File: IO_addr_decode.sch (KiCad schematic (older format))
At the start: 5 parts

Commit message: Fix wiring in root sheet
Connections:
- net ~CS_SSD1 renamed ~CS_7_SEG_0
- net ~CS_SSD2 renamed ~CS_7_SEG_1
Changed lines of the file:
@@
 $Descr A4 11693 8268
 encoding utf-8
-Sheet 14 14
+Sheet 14 15
 Title "IO Address Decode"
 Date ""
@@
 AR Path="/61AA766E/61AA7D4D" Ref="U?"  Part="1"
 AR Path="/61B01AF5/61AA7D4D" Ref="U?"  Part="1"
+AR Path="/61ABA723/61AA7D4D" Ref="U?"  Part="1"
 F 0 "U?" H 3825 3525 50  0000 C CNN
 F 1 "74LS30" H 3825 3434 50  0000 C CNN
@@
 AR Path="/61AA766E/61ABC77F" Ref="#PWR?"  Part="1"
 AR Path="/61B01AF5/61ABC77F" Ref="#PWR?"  Part="1"
+AR Path="/61ABA723/61ABC77F" Ref="#PWR?"  Part="1"
 F 0 "#PWR?" H 7500 3375 50  0001 C CNN
 F 1 "GND" H 7505 3452 50  0000 C CNN
@@
 AR Path="/61AA766E/61ABC361" Ref="#PWR?"  Part="1"
 AR Path="/61B01AF5/61ABC361" Ref="#PWR?"  Part="1"
+AR Path="/61ABA723/61ABC361" Ref="#PWR?"  Part="1"
 F 0 "#PWR?" H 7500 2175 50  0001 C CNN
 F 1 "VCC" H 7515 2498 50  0000 C CNN
@@
 AR Path="/61AA766E/61AC4663" Ref="#PWR?"  Part="1"
 AR Path="/61B01AF5/61AC4663" Ref="#PWR?"  Part="1"
+AR Path="/61ABA723/61AC4663" Ref="#PWR?"  Part="1"
 F 0 "#PWR?" H 7500 5225 50  0001 C CNN
 F 1 "GND" H 7505 5302 50  0000 C CNN
@@
 AR Path="/61AA766E/61AC466D" Ref="#PWR?"  Part="1"
 AR Path="/61B01AF5/61AC466D" Ref="#PWR?"  Part="1"
+AR Path="/61ABA723/61AC466D" Ref="#PWR?"  Part="1"
 F 0 "#PWR?" H 7500 4025 50  0001 C CNN
 F 1 "VCC" H 7515 4348 50  0000 C CNN
@@
 AR Path="/61AA766E/61AC4691" Ref="U?"  Part="1"
 AR Path="/61B01AF5/61AC4691" Ref="U?"  Part="1"
+AR Path="/61ABA723/61AC4691" Ref="U?"  Part="1"
 F 0 "U?" H 7250 5625 50  0000 C CNN
 F 1 "PAL16L8" H 7250 5525 50  0000 C CNN
@@
 AR Path="/61AA766E/61AAD950" Ref="U?"  Part="1"
 AR Path="/61B01AF5/61AAD950" Ref="U?"  Part="1"
+AR Path="/61ABA723/61AAD950" Ref="U?"  Part="1"
 F 0 "U?" H 7250 3775 50  0000 C CNN
 F 1 "PAL16L8" H 7250 3675 50  0000 C CNN
@@
 ~CS_LCD
 Text HLabel 8000 4375 2    50   Output ~ 0
-~CS_SSD1
+~CS_7_SEG_0
 Text HLabel 8000 4475 2    50   Output ~ 0
-~CS_SSD2
+~CS_7_SEG_1
 Text HLabel 8000 4575 2    50   Output ~ 0
 ~CS_LED
@@
 AR Path="/61AA766E/61AEBFAB" Ref="C?"  Part="1"
 AR Path="/61B01AF5/61AEBFAB" Ref="C?"  Part="1"
+AR Path="/61ABA723/61AEBFAB" Ref="C?"  Part="1"
 F 0 "C?" H 3365 5046 50  0000 L CNN
 F 1 "100nF" H 3365 4955 50  0000 L CNN
@@
 AR Path="/61AA766E/61AEC48E" Ref="C?"  Part="1"
 AR Path="/61B01AF5/61AEC48E" Ref="C?"  Part="1"
+AR Path="/61ABA723/61AEC48E" Ref="C?"  Part="1"
 F 0 "C?" H 3865 5046 50  0000 L CNN
 F 1 "100nF" H 3865 4955 50  0000 L CNN
@@
 AR Path="/61AA766E/61AF08F7" Ref="#PWR?"  Part="1"
 AR Path="/61B01AF5/61AF08F7" Ref="#PWR?"  Part="1"
+AR Path="/61ABA723/61AF08F7" Ref="#PWR?"  Part="1"
 F 0 "#PWR?" H 3500 4900 50  0001 C CNN
 F 1 "GND" H 3505 4977 50  0000 C CNN
@@
 AR Path="/61AA766E/61AF0CA8" Ref="#PWR?"  Part="1"
 AR Path="/61B01AF5/61AF0CA8" Ref="#PWR?"  Part="1"
+AR Path="/61ABA723/61AF0CA8" Ref="#PWR?"  Part="1"
 F 0 "#PWR?" H 3500 4700 50  0001 C CNN
 F 1 "VCC" H 3515 5023 50  0000 C CNN

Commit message: Decode BHE for IO addresses
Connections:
- net ~CS_LCD: now also U?.15 (IO5); no longer U?.12 (IO8)
- net ~CS_UART: now also U?.14 (IO6); no longer U?.13 (IO7)
- net ~BHE: now reaches U?.12 (IO8)
- net ~BHE: now also U?.12 (IO8)
- no-connect marks 4 -> 2
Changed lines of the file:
@@
 	1    0    0    -1
 $EndComp
-NoConn ~ 8000 5075
 Text HLabel 8000 2525 2    50   Output ~ 0
 ~CS_PPI1
@@
 Text HLabel 8000 3025 2    50   Output ~ 0
 ~CS_KBRD
-Text HLabel 8000 3125 2    50   Output ~ 0
+Text HLabel 8000 4875 2    50   Output ~ 0
 ~CS_UART
-Text HLabel 8000 3225 2    50   Output ~ 0
+Text HLabel 8000 4775 2    50   Output ~ 0
 ~CS_LCD
 Text HLabel 8000 4375 2    50   Output ~ 0
@@
 Text HLabel 8000 4675 2    50   Output ~ 0
 ~CS_SW
-NoConn ~ 8000 4775
-NoConn ~ 8000 4875
 NoConn ~ 8000 4975
 $Comp
@@
 Text Notes 6875 1950 0    50   ~ 0
 16L8 PAL: decode low byte
+NoConn ~ 8000 3125
 Wire Bus Line
 	6675 4150 6675 4975
@@
 Wire Bus Line
 	3200 2475 3200 3300
+Text HLabel 8000 3225 2    50   Input ~ 0
+~BHE
+Text HLabel 8000 5075 2    50   Input ~ 0
+~BHE
 $EndSCHEMATC

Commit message: General edits; removed floating inputs
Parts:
- added U?: 74LS30, symbol 74xx:74LS30
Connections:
- net HI_BYTE_FF is gone; now on net ~HI_BYTE_FF: U?.9 (I9)
- net GND: now also U?.7 (GND)
- net VCC: now also U?.14 (VCC)
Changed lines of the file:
@@
 ~HI_BYTE_FF
 Text Label 7000 5175 2    50   ~ 0
-HI_BYTE_FF
+~HI_BYTE_FF
 $Comp
 L Logic_Programmable:PAL16L8 U?
@@
 16L8 PAL: decode low byte
 NoConn ~ 8000 3125
+Text HLabel 8000 3225 2    50   Input ~ 0
+~BHE
+Text HLabel 8000 5075 2    50   Input ~ 0
+~BHE
+$Comp
+L 74xx:74LS30 U?
+U 2 1 61F51AA5
+P 4550 5050
+F 0 "U?" H 4780 5096 50  0000 L CNN
+F 1 "74LS30" H 4780 5005 50  0000 L CNN
+F 2 "" H 4550 5050 50  0001 C CNN
+F 3 "http://www.ti.com/lit/gpn/sn74LS30" H 4550 5050 50  0001 C CNN
+	2    4550 5050
+	1    0    0    -1
+$EndComp
+Wire Wire Line
+	4550 4550 3750 4550
+Wire Wire Line
+	3750 4550 3750 4850
+Connection ~ 3750 4850
+Wire Wire Line
+	4550 5550 3750 5550
+Wire Wire Line
+	3750 5550 3750 5150
 Wire Bus Line
 	6675 4150 6675 4975
@@
 Wire Bus Line
 	3200 2475 3200 3300
-Text HLabel 8000 3225 2    50   Input ~ 0
-~BHE
-Text HLabel 8000 5075 2    50   Input ~ 0
-~BHE
+Connection ~ 3750 5150
 $EndSCHEMATC

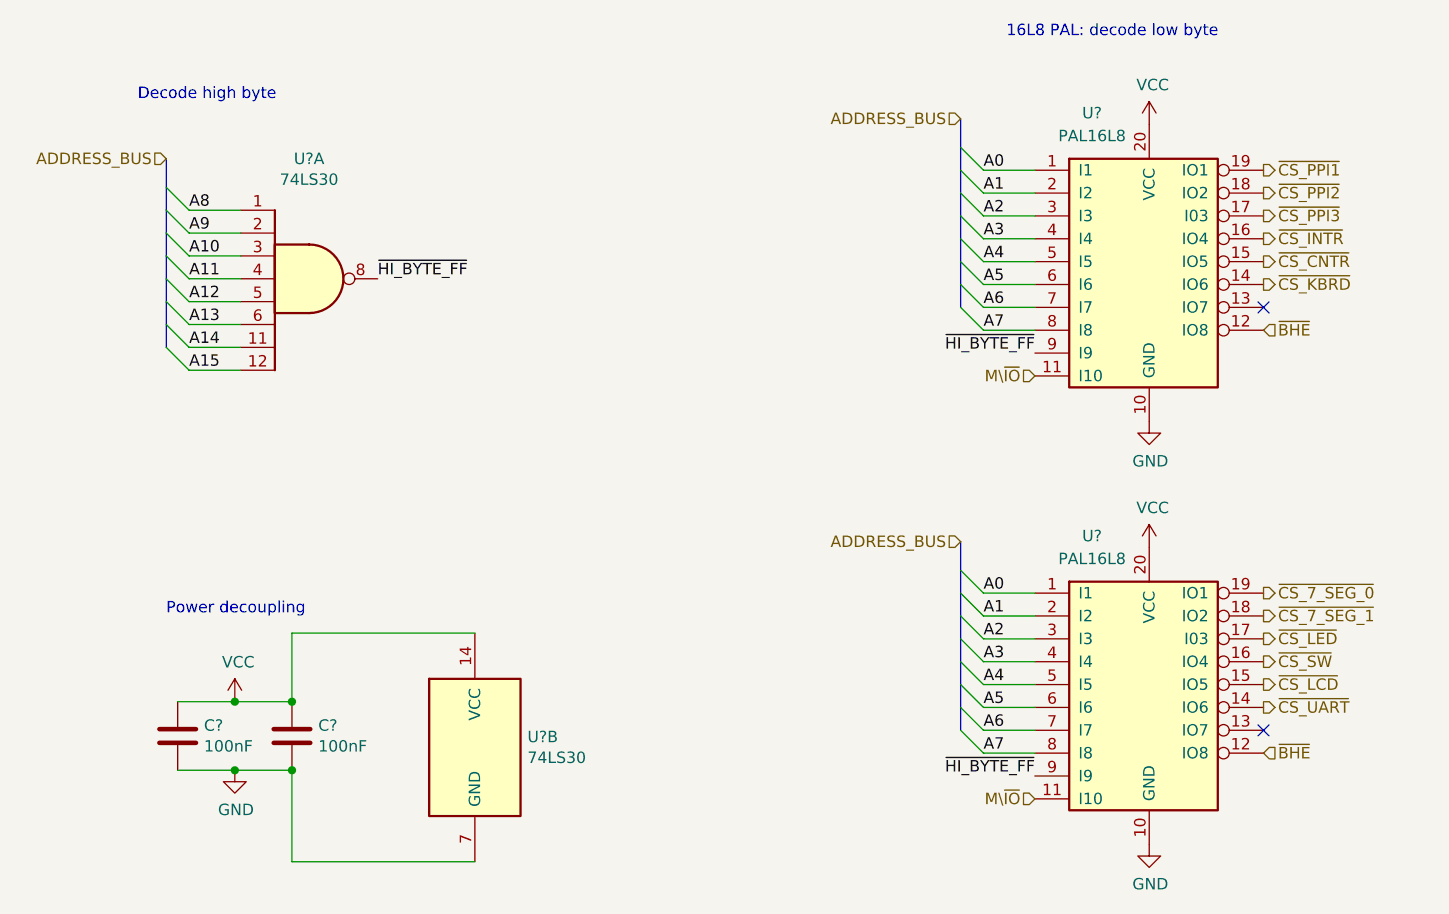
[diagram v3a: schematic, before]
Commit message: Updates to pass ERC
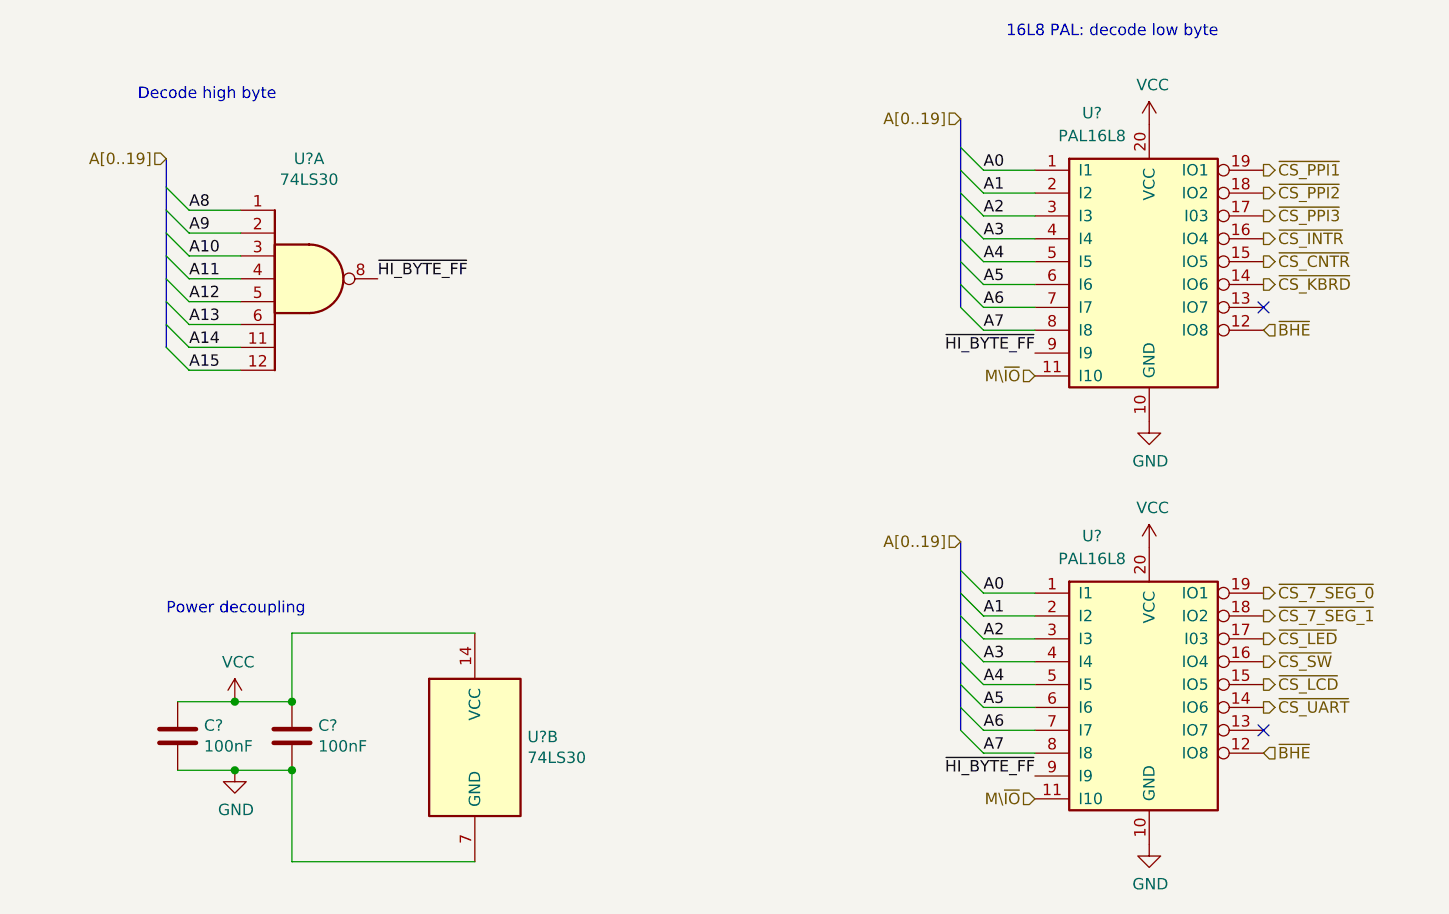
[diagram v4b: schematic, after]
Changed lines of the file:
@@
 $EndComp
 Text HLabel 3200 2475 0    50   Input ~ 0
-ADDRESS_BUS
+A[0..19]
 Text Label 4125 3000 0    50   ~ 0
 ~HI_BYTE_FF
@@
 M\~IO
 Text HLabel 6675 2300 0    50   Input ~ 0
-ADDRESS_BUS
+A[0..19]
 Entry Wire Line
 	6675 3125 6775 3225
@@
 M\~IO
 Text HLabel 6675 4150 0    50   Input ~ 0
-ADDRESS_BUS
+A[0..19]
 Entry Wire Line
 	6675 4975 6775 5075

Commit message: Assign footprints for most symbols
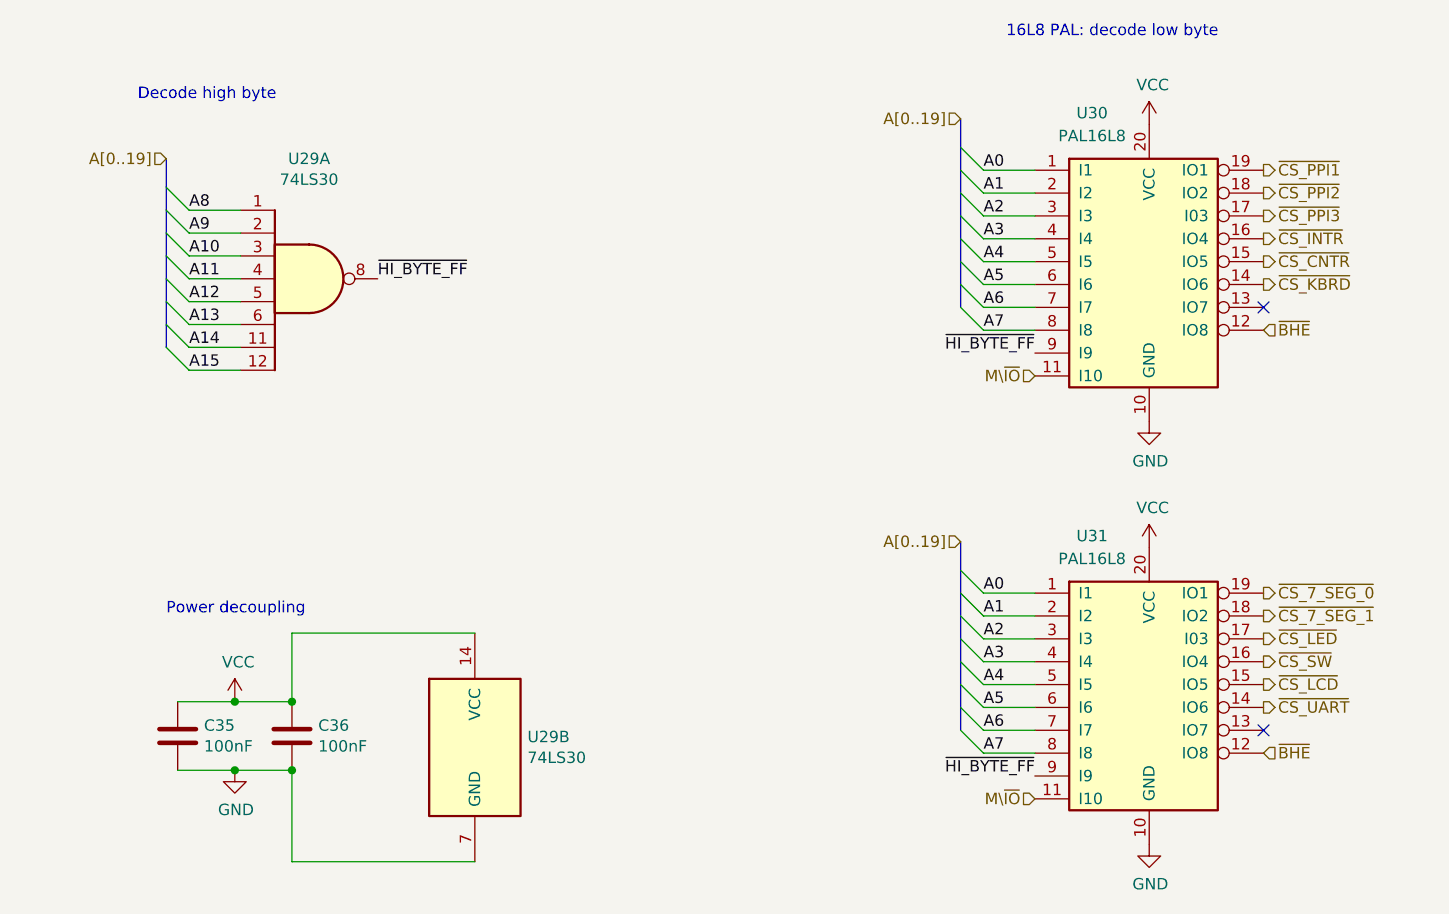
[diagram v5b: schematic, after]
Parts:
- C35, C36: renamed from C?; footprint (none) -> Capacitor_THT:C_Rect_L4.0mm_W2.5mm_P2.50mm
- U29: renamed from U?; footprint (none) -> Package_DIP:DIP-14_W7.62mm
- U30, U31: renamed from U?; footprint (none) -> Package_DIP:DIP-20_W7.62mm
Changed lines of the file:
@@
 AR Path="/61AA766E/61AA7D4D" Ref="U?"  Part="1"
 AR Path="/61B01AF5/61AA7D4D" Ref="U?"  Part="1"
-AR Path="/61ABA723/61AA7D4D" Ref="U?"  Part="1"
-F 0 "U?" H 3825 3525 50  0000 C CNN
+AR Path="/61ABA723/61AA7D4D" Ref="U29"  Part="1"
+F 0 "U29" H 3825 3525 50  0000 C CNN
 F 1 "74LS30" H 3825 3434 50  0000 C CNN
-F 2 "" H 3825 3000 50  0001 C CNN
+F 2 "Package_DIP:DIP-14_W7.62mm" H 3825 3000 50  0001 C CNN
 F 3 "http://www.ti.com/lit/gpn/sn74LS30" H 3825 3000 50  0001 C CNN
 	1    3825 3000
@@
 AR Path="/61AA766E/61ABC77F" Ref="#PWR?"  Part="1"
 AR Path="/61B01AF5/61ABC77F" Ref="#PWR?"  Part="1"
-AR Path="/61ABA723/61ABC77F" Ref="#PWR?"  Part="1"
-F 0 "#PWR?" H 7500 3375 50  0001 C CNN
+AR Path="/61ABA723/61ABC77F" Ref="#PWR0212"  Part="1"
+F 0 "#PWR0212" H 7500 3375 50  0001 C CNN
 F 1 "GND" H 7505 3452 50  0000 C CNN
 F 2 "" H 7500 3625 50  0001 C CNN
@@
 AR Path="/61AA766E/61ABC361" Ref="#PWR?"  Part="1"
 AR Path="/61B01AF5/61ABC361" Ref="#PWR?"  Part="1"
-AR Path="/61ABA723/61ABC361" Ref="#PWR?"  Part="1"
-F 0 "#PWR?" H 7500 2175 50  0001 C CNN
+AR Path="/61ABA723/61ABC361" Ref="#PWR0213"  Part="1"
+F 0 "#PWR0213" H 7500 2175 50  0001 C CNN
 F 1 "VCC" H 7515 2498 50  0000 C CNN
 F 2 "" H 7500 2325 50  0001 C CNN
@@
 AR Path="/61AA766E/61AC4663" Ref="#PWR?"  Part="1"
 AR Path="/61B01AF5/61AC4663" Ref="#PWR?"  Part="1"
-AR Path="/61ABA723/61AC4663" Ref="#PWR?"  Part="1"
-F 0 "#PWR?" H 7500 5225 50  0001 C CNN
+AR Path="/61ABA723/61AC4663" Ref="#PWR0214"  Part="1"
+F 0 "#PWR0214" H 7500 5225 50  0001 C CNN
 F 1 "GND" H 7505 5302 50  0000 C CNN
 F 2 "" H 7500 5475 50  0001 C CNN
@@
 AR Path="/61AA766E/61AC466D" Ref="#PWR?"  Part="1"
 AR Path="/61B01AF5/61AC466D" Ref="#PWR?"  Part="1"
-AR Path="/61ABA723/61AC466D" Ref="#PWR?"  Part="1"
-F 0 "#PWR?" H 7500 4025 50  0001 C CNN
+AR Path="/61ABA723/61AC466D" Ref="#PWR0215"  Part="1"
+F 0 "#PWR0215" H 7500 4025 50  0001 C CNN
 F 1 "VCC" H 7515 4348 50  0000 C CNN
 F 2 "" H 7500 4175 50  0001 C CNN
@@
 AR Path="/61AA766E/61AC4691" Ref="U?"  Part="1"
 AR Path="/61B01AF5/61AC4691" Ref="U?"  Part="1"
-AR Path="/61ABA723/61AC4691" Ref="U?"  Part="1"
-F 0 "U?" H 7250 5625 50  0000 C CNN
+AR Path="/61ABA723/61AC4691" Ref="U31"  Part="1"
+F 0 "U31" H 7250 5625 50  0000 C CNN
 F 1 "PAL16L8" H 7250 5525 50  0000 C CNN
-F 2 "" H 7500 4875 50  0001 C CNN
+F 2 "Package_DIP:DIP-20_W7.62mm" H 7500 4875 50  0001 C CNN
 F 3 "" H 7500 4875 50  0001 C CNN
 	1    7500 4875
@@
 AR Path="/61AA766E/61AAD950" Ref="U?"  Part="1"
 AR Path="/61B01AF5/61AAD950" Ref="U?"  Part="1"
-AR Path="/61ABA723/61AAD950" Ref="U?"  Part="1"
-F 0 "U?" H 7250 3775 50  0000 C CNN
+AR Path="/61ABA723/61AAD950" Ref="U30"  Part="1"
+F 0 "U30" H 7250 3775 50  0000 C CNN
 F 1 "PAL16L8" H 7250 3675 50  0000 C CNN
-F 2 "" H 7500 3025 50  0001 C CNN
+F 2 "Package_DIP:DIP-20_W7.62mm" H 7500 3025 50  0001 C CNN
 F 3 "" H 7500 3025 50  0001 C CNN
 	1    7500 3025
@@
 AR Path="/61AA766E/61AEBFAB" Ref="C?"  Part="1"
 AR Path="/61B01AF5/61AEBFAB" Ref="C?"  Part="1"
-AR Path="/61ABA723/61AEBFAB" Ref="C?"  Part="1"
-F 0 "C?" H 3365 5046 50  0000 L CNN
+AR Path="/61ABA723/61AEBFAB" Ref="C35"  Part="1"
+F 0 "C35" H 3365 5046 50  0000 L CNN
 F 1 "100nF" H 3365 4955 50  0000 L CNN
-F 2 "" H 3288 4850 50  0001 C CNN
+F 2 "Capacitor_THT:C_Rect_L4.0mm_W2.5mm_P2.50mm" H 3288 4850 50  0001 C CNN
 F 3 "~" H 3250 5000 50  0001 C CNN
 	1    3250 5000
@@
 AR Path="/61AA766E/61AEC48E" Ref="C?"  Part="1"
 AR Path="/61B01AF5/61AEC48E" Ref="C?"  Part="1"
-AR Path="/61ABA723/61AEC48E" Ref="C?"  Part="1"
-F 0 "C?" H 3865 5046 50  0000 L CNN
+AR Path="/61ABA723/61AEC48E" Ref="C36"  Part="1"
+F 0 "C36" H 3865 5046 50  0000 L CNN
 F 1 "100nF" H 3865 4955 50  0000 L CNN
-F 2 "" H 3788 4850 50  0001 C CNN
+F 2 "Capacitor_THT:C_Rect_L4.0mm_W2.5mm_P2.50mm" H 3788 4850 50  0001 C CNN
 F 3 "~" H 3750 5000 50  0001 C CNN
 	1    3750 5000
@@
 AR Path="/61AA766E/61AF08F7" Ref="#PWR?"  Part="1"
 AR Path="/61B01AF5/61AF08F7" Ref="#PWR?"  Part="1"
-AR Path="/61ABA723/61AF08F7" Ref="#PWR?"  Part="1"
-F 0 "#PWR?" H 3500 4900 50  0001 C CNN
+AR Path="/61ABA723/61AF08F7" Ref="#PWR0216"  Part="1"
+F 0 "#PWR0216" H 3500 4900 50  0001 C CNN
 F 1 "GND" H 3505 4977 50  0000 C CNN
 F 2 "" H 3500 5150 50  0001 C CNN
@@
 AR Path="/61AA766E/61AF0CA8" Ref="#PWR?"  Part="1"
 AR Path="/61B01AF5/61AF0CA8" Ref="#PWR?"  Part="1"
-AR Path="/61ABA723/61AF0CA8" Ref="#PWR?"  Part="1"
-F 0 "#PWR?" H 3500 4700 50  0001 C CNN
+AR Path="/61ABA723/61AF0CA8" Ref="#PWR0217"  Part="1"
+F 0 "#PWR0217" H 3500 4700 50  0001 C CNN
 F 1 "VCC" H 3515 5023 50  0000 C CNN
 F 2 "" H 3500 4850 50  0001 C CNN
@@
 ~BHE
 $Comp
-L 74xx:74LS30 U?
+L 74xx:74LS30 U29
 U 2 1 61F51AA5
 P 4550 5050
-F 0 "U?" H 4780 5096 50  0000 L CNN
+F 0 "U29" H 4780 5096 50  0000 L CNN
 F 1 "74LS30" H 4780 5005 50  0000 L CNN
-F 2 "" H 4550 5050 50  0001 C CNN
+F 2 "Package_DIP:DIP-14_W7.62mm" H 4550 5050 50  0001 C CNN
 F 3 "http://www.ti.com/lit/gpn/sn74LS30" H 4550 5050 50  0001 C CNN
 	2    4550 5050
@@
 Wire Wire Line
 	3750 5550 3750 5150
+Connection ~ 3750 5150
 Wire Bus Line
 	6675 4150 6675 4975
@@
 Wire Bus Line
 	3200 2475 3200 3300
-Connection ~ 3750 5150
 $EndSCHEMATC

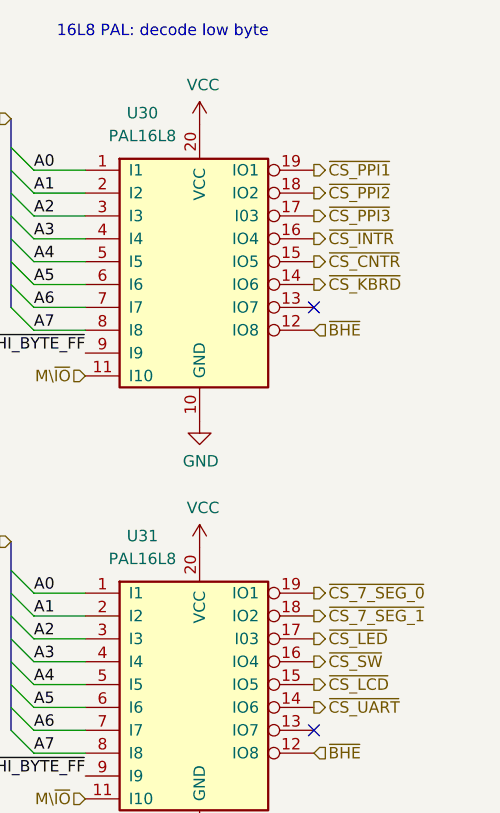
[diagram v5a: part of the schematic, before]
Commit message: Route data bus lines, most chip selects
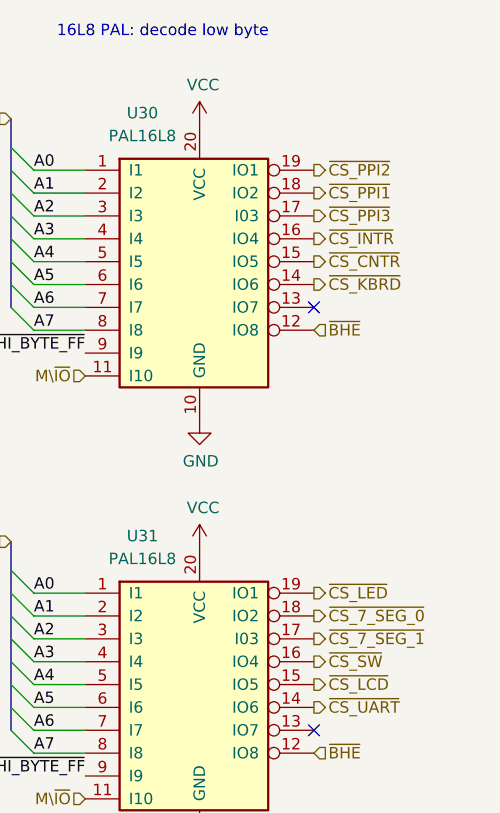
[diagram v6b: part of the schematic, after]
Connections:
- net ~CS_7_SEG_0: now also U31.18 (IO2); no longer U31.19 (IO1)
- net ~CS_7_SEG_1: now also U31.17 (I03); no longer U31.18 (IO2)
- net ~CS_LED: now also U31.19 (IO1); no longer U31.17 (I03)
- net ~CS_PPI1: now also U30.18 (IO2); no longer U30.19 (IO1)
- net ~CS_PPI2: now also U30.19 (IO1); no longer U30.18 (IO2)
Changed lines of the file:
@@
 	1    0    0    -1
 $EndComp
+Text HLabel 8000 2625 2    50   Output ~ 0
+~CS_PPI1
 Text HLabel 8000 2525 2    50   Output ~ 0
-~CS_PPI1
-Text HLabel 8000 2625 2    50   Output ~ 0
 ~CS_PPI2
 Text HLabel 8000 2725 2    50   Output ~ 0
@@
 Text HLabel 8000 4775 2    50   Output ~ 0
 ~CS_LCD
+Text HLabel 8000 4475 2    50   Output ~ 0
+~CS_7_SEG_0
+Text HLabel 8000 4575 2    50   Output ~ 0
+~CS_7_SEG_1
 Text HLabel 8000 4375 2    50   Output ~ 0
-~CS_7_SEG_0
-Text HLabel 8000 4475 2    50   Output ~ 0
-~CS_7_SEG_1
-Text HLabel 8000 4575 2    50   Output ~ 0
 ~CS_LED
 Text HLabel 8000 4675 2    50   Output ~ 0
